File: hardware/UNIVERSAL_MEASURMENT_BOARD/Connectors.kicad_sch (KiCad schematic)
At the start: 44 parts, among them J1 FTSH-107-01-L-D-K, J2 2606-1110_010-000, J3 2606-1110_010-000, J4 Strain Relief, J5 Strain Relief, J6 Strain Relief, J7 Strain Relief, J8 2606-1110_010-000, J9 2606-1110_010-000, U16 ESDS304DBVR, U17 ESDS304DBVR

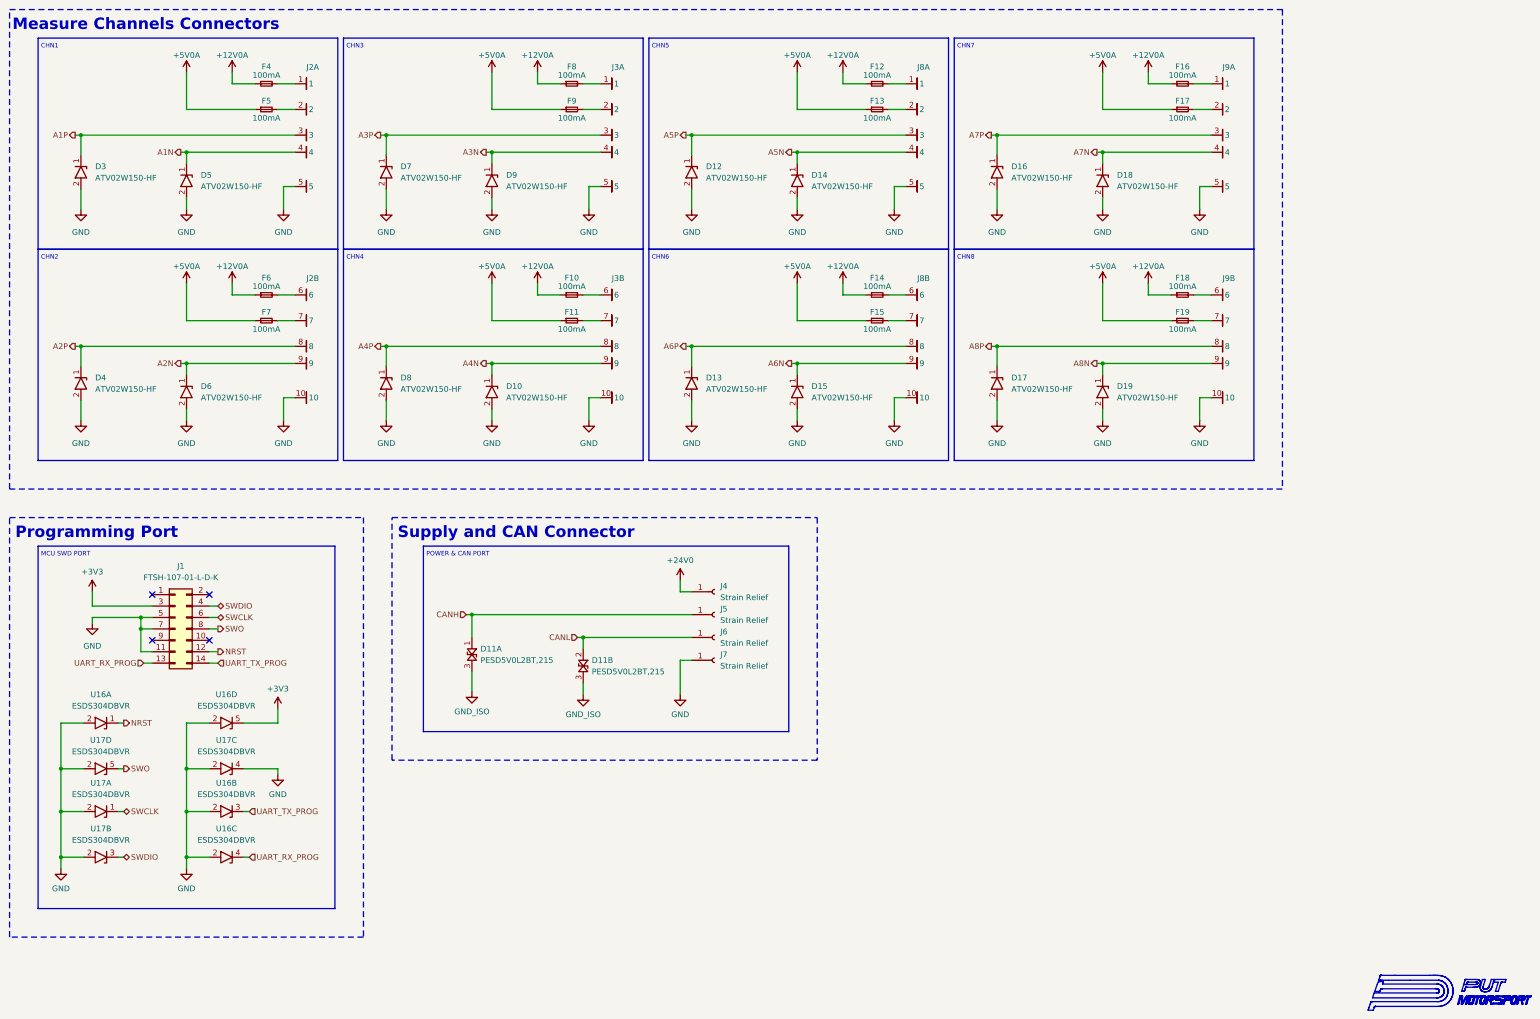
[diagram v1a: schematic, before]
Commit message: Reduced PCB dimensions, working on power section
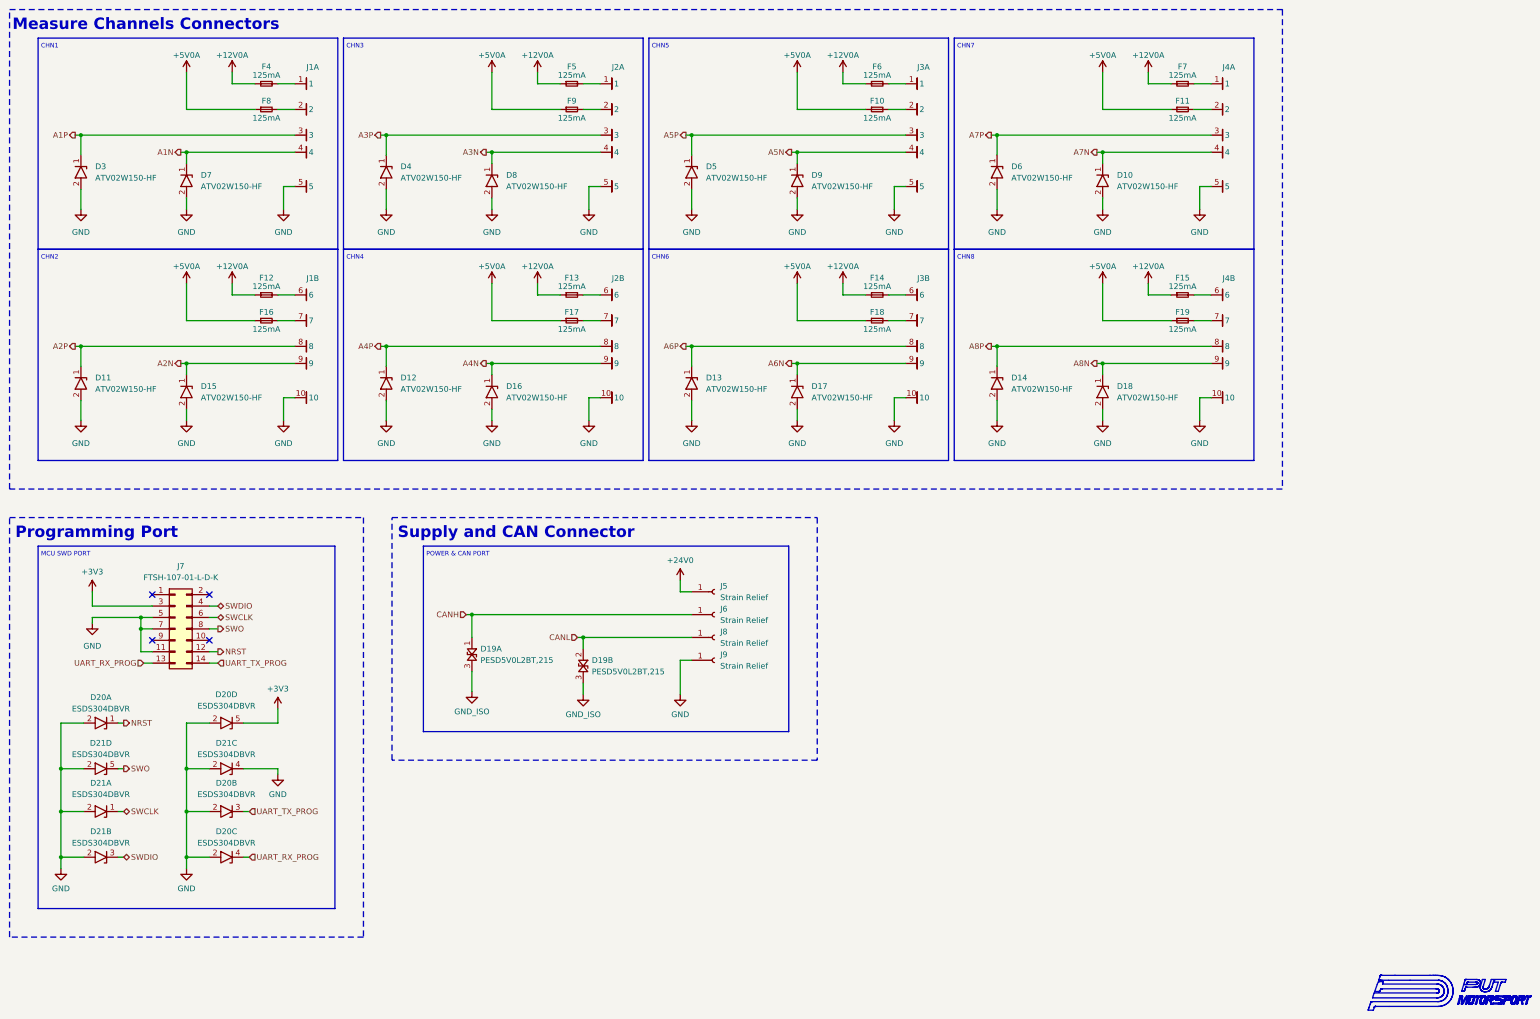
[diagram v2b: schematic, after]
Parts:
- removed U16, U17: ESDS304DBVR, SOT95P280X145-5N, symbol ESDS304DBVR:ESDS304DBVR
- added D20, D21: ESDS304DBVR, SOT95P280X145-5N, symbol ESDS304DBVR:ESDS304DBVR
- F10: renamed from F13; value 100mA -> 125mA
- F11: renamed from F17; value 100mA -> 125mA
- F12: renamed from F6; value 100mA -> 125mA
- F13: renamed from F10; value 100mA -> 125mA
- F14, F19, F4, F9: value 100mA -> 125mA
- F15: renamed from F18; value 100mA -> 125mA
- F16: renamed from F7; value 100mA -> 125mA
- F17: renamed from F11; value 100mA -> 125mA
- F18: renamed from F15; value 100mA -> 125mA
- F5: renamed from F8; value 100mA -> 125mA
- F6: renamed from F12; value 100mA -> 125mA
- F7: renamed from F16; value 100mA -> 125mA
- F8: renamed from F5; value 100mA -> 125mA
- renumbered D18 to D10, D4 to D11, D8 to D12, D17 to D14, D6 to D15, D10 to D16, D15 to D17, D19 to D18, D11 to D19, D7 to D4, D12 to D5, D16 to D6, D5 to D7, D9 to D8, D14 to D9, J2 to J1, J3 to J2, J8 to J3, J9 to J4, J4 to J5, J5 to J6, J1 to J7, J6 to J8, J7 to J9
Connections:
- net +3V3: now also D20.5
- net GND: now also D20.2, D20.2, D20.2, D20.2, D21.2, D21.2, D21.2, D21.2, D21.4
- net NRST: now also D20.1
- net SWCLK: now also D21.1
- net SWDIO: now also D21.3
- net SWO: now also D21.5
- net UART_RX_PROG: now also D20.4
- net UART_TX_PROG: now also D20.3
